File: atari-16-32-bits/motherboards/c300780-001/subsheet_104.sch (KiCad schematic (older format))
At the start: 0 parts

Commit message: sheet 1 done
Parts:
- added C100: 10uF, symbol Device:CP1
- added C101: 0.01uF, symbol Device:CP1
- added C102: 22uF, symbol Device:CP1
- added D100: 1N914, symbol Device:D
- added R100: 10K, symbol Device:R_US
- added R101: 12K, symbol Device:R_US
- added S100: RESET switch, symbol Switch:SW_SPDT
- added U104: LM555_TIMER_PHY, Package_DIP:DIP-8_W7.62mm_LongPads, symbol lm555:LM555_TIMER_PHY
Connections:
- new net CV: C101.1, U104.5 (CTLVLT)
- new net DxT: C102.1, R101.2, U104.6 (THRESHOLD), U104.7 (DISCHARGE)
- new net GND: C100.2, C101.2, C102.2, S100.3 (C), U104.1 (GND)
- new net RESET: U104.3 (OUTPUT)
- new net TRIG: C100.1, D100.2 (A), R100.2, S100.2 (B), U104.2 (TRIGGER)
- new net VCC: D100.1 (K), R100.1, R101.1, U104.4 (~RESET~), U104.8 (Vcc)
- no-connect marks 0 -> 1
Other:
- note added: "Circuitry for Control Voltage"
- note added: "Circuitry for Trigger"
- note added: "Circuitry for \nDischarge & Threshold"
- note added: "RESET is sent to U210 \nto drive XRESET & XHALT"
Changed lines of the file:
@@
 EELAYER 30 0
 EELAYER END
-$Descr A4 11693 8268
+$Descr A4 8268 11693 portrait
 encoding utf-8
 Sheet 7 14
@@
 Comment4 ""
 $EndDescr
+$Comp
+L lm555:LM555_TIMER_PHY U104
+U 1 1 608BDB9F
+P 4300 1750
+F 0 "U104" H 3750 2200 50  0000 L TNN
+F 1 "LM555_TIMER_PHY" H 3750 2100 50  0000 L TNB
+F 2 "Package_DIP:DIP-8_W7.62mm_LongPads" H 3750 2300 50  0001 L TNN
+F 3 "https://www.ti.com/lit/ds/symlink/lm555.pdf" H 3750 2400 50  0001 L TNN
+	1    4300 1750
+	1    0    0    -1
+$EndComp
+Text Label 3250 1600 0    50   ~ 0
+GND
+Text Label 3250 1700 0    50   ~ 0
+TRIG
+Text Label 3250 1900 0    50   ~ 0
+VCC
+Text Label 5350 1600 2    50   ~ 0
+VCC
+Text Label 5350 1700 2    50   ~ 0
+DxT
+Text Label 5350 1800 2    50   ~ 0
+DxT
+Text Label 5350 1900 2    50   ~ 0
+CV
+Wire Wire Line
+	3250 1600 3450 1600
+Wire Wire Line
+	3250 1700 3450 1700
+Wire Wire Line
+	3250 1800 3450 1800
+Wire Wire Line
+	3250 1900 3450 1900
+Wire Wire Line
+	5150 1600 5350 1600
+Wire Wire Line
+	5150 1700 5350 1700
+Wire Wire Line
+	5150 1800 5350 1800
+Wire Wire Line
+	5150 1900 5350 1900
+NoConn ~ 2050 1700
+$Comp
+L Switch:SW_SPDT S100
+U 1 1 608C05EE
+P 1850 1800
+F 0 "S100" H 1850 1970 50  0000 C CNN
+F 1 "RESET switch" H 1850 1600 50  0000 C CNN
+F 2 "" H 1850 1800 50  0001 C CNN
+F 3 "~" H 1850 1800 50  0001 C CNN
+	1    1850 1800
+	1    0    0    -1
+$EndComp
+Text Label 1450 1800 0    50   ~ 0
+TRIG
+Wire Wire Line
+	1450 1800 1650 1800
+Text Label 2250 1900 2    50   ~ 0
+GND
+Wire Wire Line
+	2050 1900 2250 1900
+$Comp
+L Device:R_US R100
+U 1 1 608C1635
+P 1850 2300
+F 0 "R100" V 1950 2300 50  0000 C CNN
+F 1 "10K" V 1750 2300 50  0000 C CNN
+F 2 "" V 1890 2290 50  0001 C CNN
+F 3 "~" H 1850 2300 50  0001 C CNN
+	1    1850 2300
+	0    1    1    0
+$EndComp
+Text Label 2200 2300 2    50   ~ 0
+VCC
+Text Label 1500 2300 0    50   ~ 0
+TRIG
+$Comp
+L Device:CP1 C100
+U 1 1 608C1A6C
+P 1850 3300
+F 0 "C100" V 1700 3200 50  0000 L CNN
+F 1 "10uF" V 2000 3200 50  0000 L CNN
+F 2 "" H 1850 3300 50  0001 C CNN
+F 3 "~" H 1850 3300 50  0001 C CNN
+	1    1850 3300
+	0    -1   -1   0
+$EndComp
+Text Label 1500 3300 0    50   ~ 0
+TRIG
+Text Label 2200 3300 2    50   ~ 0
+GND
+$Comp
+L Device:D D100
+U 1 1 608C24B7
+P 1850 2800
+F 0 "D100" H 1850 2900 50  0000 C CNN
+F 1 "1N914" H 1850 2700 50  0000 C CNN
+F 2 "" H 1850 2800 50  0001 C CNN
+F 3 "~" H 1850 2800 50  0001 C CNN
+	1    1850 2800
+	-1   0    0    1
+$EndComp
+Text Label 1500 2800 0    50   ~ 0
+TRIG
+Text Label 2200 2800 2    50   ~ 0
+VCC
+Wire Wire Line
+	1500 2300 1700 2300
+Wire Wire Line
+	2000 2300 2200 2300
+Wire Wire Line
+	1500 2800 1700 2800
+Wire Wire Line
+	2000 2800 2200 2800
+Wire Wire Line
+	1500 3300 1700 3300
+Wire Wire Line
+	2000 3300 2200 3300
+$Comp
+L Device:CP1 C101
+U 1 1 608C7F71
+P 6350 3350
+F 0 "C101" V 6200 3250 50  0000 L CNN
+F 1 "0.01uF" V 6500 3250 50  0000 L CNN
+F 2 "" H 6350 3350 50  0001 C CNN
+F 3 "~" H 6350 3350 50  0001 C CNN
+	1    6350 3350
+	0    -1   -1   0
+$EndComp
+Text Label 6000 3350 0    50   ~ 0
+CV
+Text Label 6700 3350 2    50   ~ 0
+GND
+Wire Wire Line
+	6000 3350 6200 3350
+Wire Wire Line
+	6500 3350 6700 3350
+$Comp
+L Device:CP1 C102
+U 1 1 608C88D5
+P 6350 2350
+F 0 "C102" V 6200 2250 50  0000 L CNN
+F 1 "22uF" V 6500 2250 50  0000 L CNN
+F 2 "" H 6350 2350 50  0001 C CNN
+F 3 "~" H 6350 2350 50  0001 C CNN
+	1    6350 2350
+	0    -1   -1   0
+$EndComp
+Text Label 6000 2350 0    50   ~ 0
+DxT
+Text Label 6700 2350 2    50   ~ 0
+GND
+Wire Wire Line
+	6000 2350 6200 2350
+Wire Wire Line
+	6500 2350 6700 2350
+$Comp
+L Device:R_US R101
+U 1 1 608C9171
+P 6350 1850
+F 0 "R101" V 6450 1850 50  0000 C CNN
+F 1 "12K" V 6250 1850 50  0000 C CNN
+F 2 "" V 6390 1840 50  0001 C CNN
+F 3 "~" H 6350 1850 50  0001 C CNN
+	1    6350 1850
+	0    1    1    0
+$EndComp
+Text Label 6700 1850 2    50   ~ 0
+VCC
+Text Label 6000 1850 0    50   ~ 0
+DxT
+Wire Wire Line
+	6000 1850 6200 1850
+Wire Wire Line
+	6500 1850 6700 1850
+Text GLabel 3250 1800 0    50   Output ~ 0
+RESET
+Text Notes 1450 1500 0    50   ~ 0
+Circuitry for Trigger
+Text Notes 5900 1600 0    50   ~ 0
+Circuitry for \nDischarge & Threshold
+Text Notes 5800 3050 0    50   ~ 0
+Circuitry for Control Voltage
+Text Notes 3000 2250 0    50   ~ 0
+RESET is sent to U210 \nto drive XRESET & XHALT
 $EndSCHEMATC

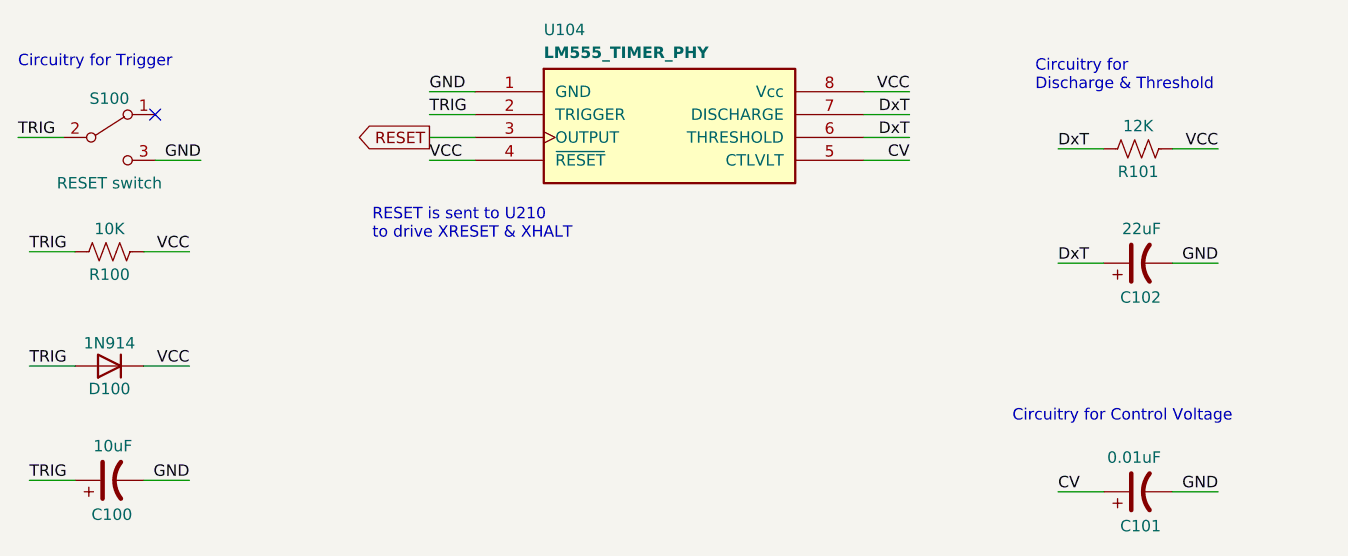
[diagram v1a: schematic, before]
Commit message: reorganized sheets
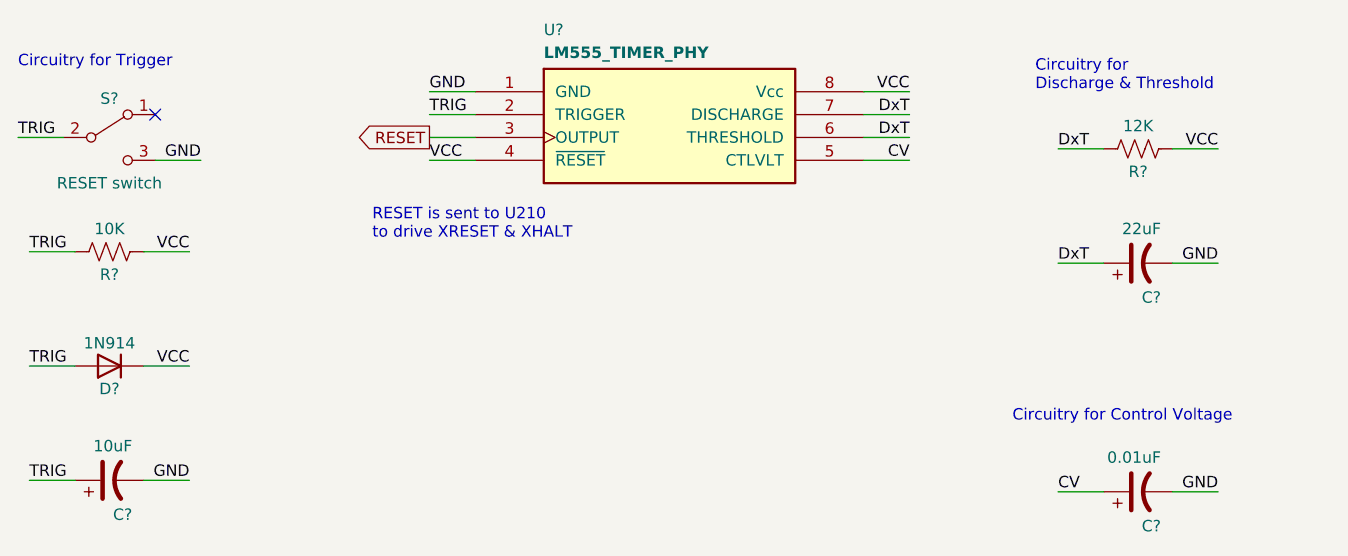
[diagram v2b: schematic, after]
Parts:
- renumbered C100 to C?, C101 to C?, C102 to C?, D100 to D?, R100 to R?, R101 to R?, S100 to S?, U104 to U?
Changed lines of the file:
@@
 $Descr A4 8268 11693 portrait
 encoding utf-8
-Sheet 7 14
+Sheet 11 8
 Title ""
 Date ""
@@
 $EndDescr
 $Comp
-L lm555:LM555_TIMER_PHY U104
+L lm555:LM555_TIMER_PHY U?
 U 1 1 608BDB9F
 P 4300 1750
-F 0 "U104" H 3750 2200 50  0000 L TNN
+F 0 "U?" H 3750 2200 50  0000 L TNN
 F 1 "LM555_TIMER_PHY" H 3750 2100 50  0000 L TNB
 F 2 "Package_DIP:DIP-8_W7.62mm_LongPads" H 3750 2300 50  0001 L TNN
@@
 NoConn ~ 2050 1700
 $Comp
-L Switch:SW_SPDT S100
+L Switch:SW_SPDT S?
 U 1 1 608C05EE
 P 1850 1800
-F 0 "S100" H 1850 1970 50  0000 C CNN
+F 0 "S?" H 1850 1970 50  0000 C CNN
 F 1 "RESET switch" H 1850 1600 50  0000 C CNN
 F 2 "" H 1850 1800 50  0001 C CNN
@@
 	2050 1900 2250 1900
 $Comp
-L Device:R_US R100
+L Device:R_US R?
 U 1 1 608C1635
 P 1850 2300
-F 0 "R100" V 1950 2300 50  0000 C CNN
+F 0 "R?" V 1950 2300 50  0000 C CNN
 F 1 "10K" V 1750 2300 50  0000 C CNN
 F 2 "" V 1890 2290 50  0001 C CNN
@@
 TRIG
 $Comp
-L Device:CP1 C100
+L Device:CP1 C?
 U 1 1 608C1A6C
 P 1850 3300
-F 0 "C100" V 1700 3200 50  0000 L CNN
+F 0 "C?" V 1700 3200 50  0000 L CNN
 F 1 "10uF" V 2000 3200 50  0000 L CNN
 F 2 "" H 1850 3300 50  0001 C CNN
@@
 GND
 $Comp
-L Device:D D100
+L Device:D D?
 U 1 1 608C24B7
 P 1850 2800
-F 0 "D100" H 1850 2900 50  0000 C CNN
+F 0 "D?" H 1850 2900 50  0000 C CNN
 F 1 "1N914" H 1850 2700 50  0000 C CNN
 F 2 "" H 1850 2800 50  0001 C CNN
@@
 	2000 3300 2200 3300
 $Comp
-L Device:CP1 C101
+L Device:CP1 C?
 U 1 1 608C7F71
 P 6350 3350
-F 0 "C101" V 6200 3250 50  0000 L CNN
+F 0 "C?" V 6200 3250 50  0000 L CNN
 F 1 "0.01uF" V 6500 3250 50  0000 L CNN
 F 2 "" H 6350 3350 50  0001 C CNN
@@
 	6500 3350 6700 3350
 $Comp
-L Device:CP1 C102
+L Device:CP1 C?
 U 1 1 608C88D5
 P 6350 2350
-F 0 "C102" V 6200 2250 50  0000 L CNN
+F 0 "C?" V 6200 2250 50  0000 L CNN
 F 1 "22uF" V 6500 2250 50  0000 L CNN
 F 2 "" H 6350 2350 50  0001 C CNN
@@
 	6500 2350 6700 2350
 $Comp
-L Device:R_US R101
+L Device:R_US R?
 U 1 1 608C9171
 P 6350 1850
-F 0 "R101" V 6450 1850 50  0000 C CNN
+F 0 "R?" V 6450 1850 50  0000 C CNN
 F 1 "12K" V 6250 1850 50  0000 C CNN
 F 2 "" V 6390 1840 50  0001 C CNN

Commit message: re-annotate component following move of subsheets in schematics
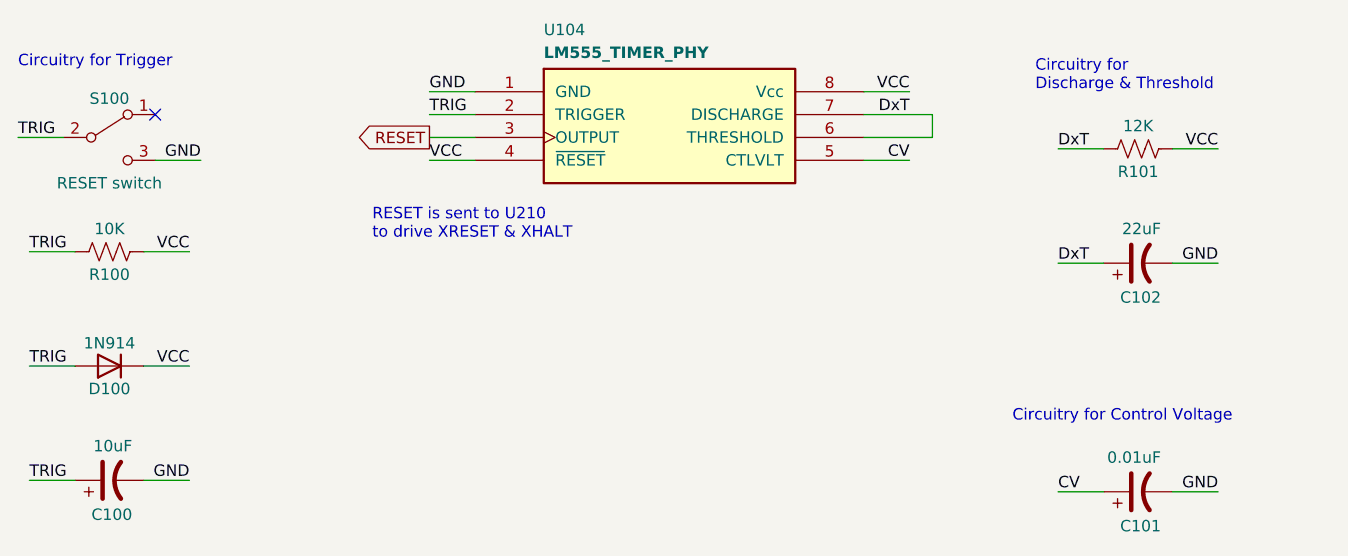
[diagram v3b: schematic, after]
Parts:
- gave numbers to parts that had none: 8
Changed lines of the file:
@@
 $Descr A4 8268 11693 portrait
 encoding utf-8
-Sheet 11 8
+Sheet 5 9
 Title ""
 Date ""
@@
 $EndDescr
 $Comp
-L lm555:LM555_TIMER_PHY U?
+L lm555:LM555_TIMER_PHY U104
 U 1 1 608BDB9F
 P 4300 1750
-F 0 "U?" H 3750 2200 50  0000 L TNN
+F 0 "U104" H 3750 2200 50  0000 L TNN
 F 1 "LM555_TIMER_PHY" H 3750 2100 50  0000 L TNB
 F 2 "Package_DIP:DIP-8_W7.62mm_LongPads" H 3750 2300 50  0001 L TNN
@@
 Text Label 5350 1700 2    50   ~ 0
 DxT
-Text Label 5350 1800 2    50   ~ 0
-DxT
 Text Label 5350 1900 2    50   ~ 0
 CV
@@
 	5150 1600 5350 1600
 Wire Wire Line
-	5150 1700 5350 1700
-Wire Wire Line
-	5150 1800 5350 1800
-Wire Wire Line
 	5150 1900 5350 1900
 NoConn ~ 2050 1700
 $Comp
-L Switch:SW_SPDT S?
+L Switch:SW_SPDT S100
 U 1 1 608C05EE
 P 1850 1800
-F 0 "S?" H 1850 1970 50  0000 C CNN
+F 0 "S100" H 1850 1970 50  0000 C CNN
 F 1 "RESET switch" H 1850 1600 50  0000 C CNN
 F 2 "" H 1850 1800 50  0001 C CNN
@@
 	2050 1900 2250 1900
 $Comp
-L Device:R_US R?
+L Device:R_US R100
 U 1 1 608C1635
 P 1850 2300
-F 0 "R?" V 1950 2300 50  0000 C CNN
+F 0 "R100" V 1950 2300 50  0000 C CNN
 F 1 "10K" V 1750 2300 50  0000 C CNN
 F 2 "" V 1890 2290 50  0001 C CNN
@@
 TRIG
 $Comp
-L Device:CP1 C?
+L Device:CP1 C100
 U 1 1 608C1A6C
 P 1850 3300
-F 0 "C?" V 1700 3200 50  0000 L CNN
+F 0 "C100" V 1700 3200 50  0000 L CNN
 F 1 "10uF" V 2000 3200 50  0000 L CNN
 F 2 "" H 1850 3300 50  0001 C CNN
@@
 GND
 $Comp
-L Device:D D?
+L Device:D D100
 U 1 1 608C24B7
 P 1850 2800
-F 0 "D?" H 1850 2900 50  0000 C CNN
+F 0 "D100" H 1850 2900 50  0000 C CNN
 F 1 "1N914" H 1850 2700 50  0000 C CNN
 F 2 "" H 1850 2800 50  0001 C CNN
@@
 	2000 3300 2200 3300
 $Comp
-L Device:CP1 C?
+L Device:CP1 C101
 U 1 1 608C7F71
 P 6350 3350
-F 0 "C?" V 6200 3250 50  0000 L CNN
+F 0 "C101" V 6200 3250 50  0000 L CNN
 F 1 "0.01uF" V 6500 3250 50  0000 L CNN
 F 2 "" H 6350 3350 50  0001 C CNN
@@
 	6500 3350 6700 3350
 $Comp
-L Device:CP1 C?
+L Device:CP1 C102
 U 1 1 608C88D5
 P 6350 2350
-F 0 "C?" V 6200 2250 50  0000 L CNN
+F 0 "C102" V 6200 2250 50  0000 L CNN
 F 1 "22uF" V 6500 2250 50  0000 L CNN
 F 2 "" H 6350 2350 50  0001 C CNN
@@
 	6500 2350 6700 2350
 $Comp
-L Device:R_US R?
+L Device:R_US R101
 U 1 1 608C9171
 P 6350 1850
-F 0 "R?" V 6450 1850 50  0000 C CNN
+F 0 "R101" V 6450 1850 50  0000 C CNN
 F 1 "12K" V 6250 1850 50  0000 C CNN
 F 2 "" V 6390 1840 50  0001 C CNN
@@
 Text Notes 3000 2250 0    50   ~ 0
 RESET is sent to U210 \nto drive XRESET & XHALT
+Wire Wire Line
+	5450 1700 5450 1800
+Wire Wire Line
+	5150 1700 5450 1700
+Wire Wire Line
+	5150 1800 5450 1800
 $EndSCHEMATC
